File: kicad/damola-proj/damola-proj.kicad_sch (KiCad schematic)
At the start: 37 parts, among them U1 DRV8833PWPR, U2 MT3608, U3 DRV8833PWPR, U4 TPS63020DSJR, U5 TPS63020

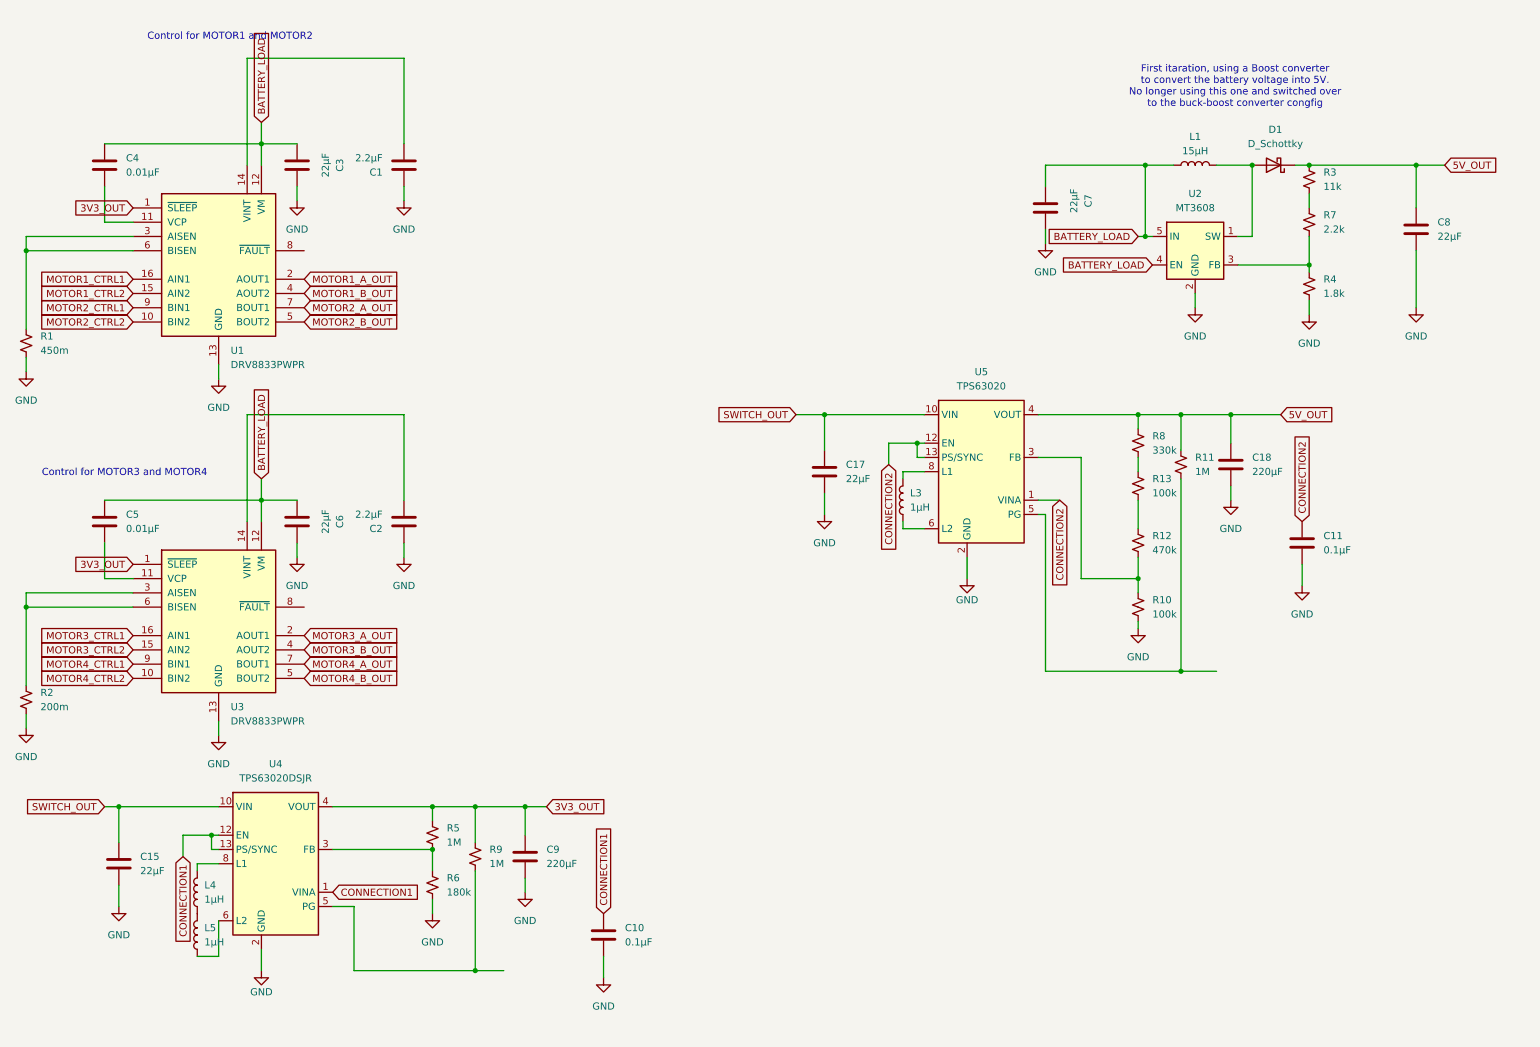
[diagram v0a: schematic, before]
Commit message: combine schematics, optimize damolas schematic, fixes, part assignment, pcb population
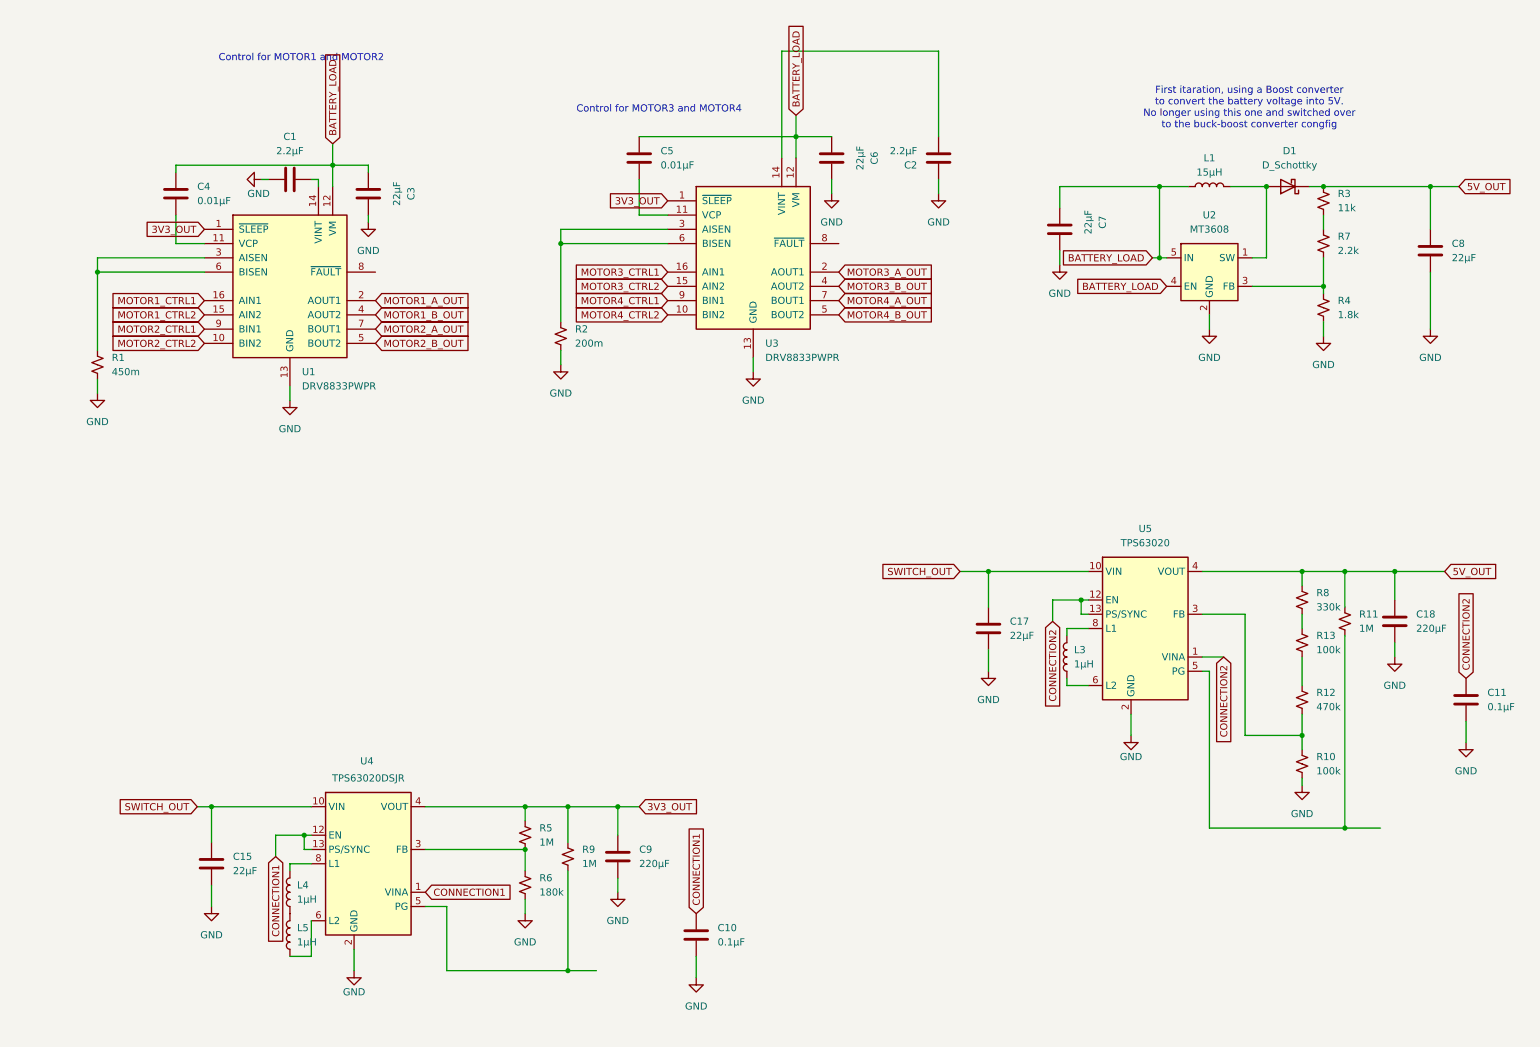
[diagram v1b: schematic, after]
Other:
- moved on the sheet: C1, C10, C11, C15, C17, C18, C2, C3, C4, C5, C6, C7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

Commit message: I believe this should sync my changes
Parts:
- added Q3, Q6: AO3401A, Package_TO_SOT_SMD:SOT-23, symbol Transistor_FET:AO3401A
- added Q4, Q5: AO3400A, Package_TO_SOT_SMD:SOT-23, symbol Transistor_FET:AO3400A
- added R14, R15: 10k, Resistor_SMD:R_0603_1608Metric_Pad0.98x0.95mm_HandSolder, symbol Device:R
- added R16, R18: 1M, Resistor_SMD:R_0603_1608Metric_Pad0.98x0.95mm_HandSolder, symbol Device:R
- added SW2: SW_SPDT, MyLibrary:SS-12D11G3R, symbol Switch:SW_SPDT
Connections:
- net 5V_OUT: now also Q3.2 (S), Q6.2 (S), R16.1, R18.1
- net GND: now also Q4.2 (S), Q5.2 (S)
- new net: Q5.3 (D), Q6.1 (G), R18.2
- new net: Q5.1 (G), R15.2
- new net: Q3.1 (G), Q4.3 (D), R16.2
- new net: Q4.1 (G), R14.2
- new net BATTERY: SW2.2 (B)
- new net BATTERY_POWER: SW2.3 (C)
- new net CHARGE_BATTERY: SW2.1 (A)
- new net CTRL_EXT_LOAD1: R14.1
- new net CTRL_EXT_LOAD2: R15.1
- new net EXT_LOAD1_OUT: Q3.3 (D)
- new net EXT_LOAD2_OUT: Q6.3 (D)
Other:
- note added: "3V3 and 5V out circuit"
- note added: "External Load switches"
- note added: "Motor control circuit for the Prushed DC motors and the Auxiliary motors."
- note added: "System Power Switch"
- title: (none) -> Micromouse Power Board
- moved on the sheet: C1, C10, C11, C15, C17, C18, C2, C3, C4, C5, C6, C7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
